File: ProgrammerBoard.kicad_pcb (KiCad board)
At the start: 2 copper layers, 11 parts, among them IC1 FT232RL, J1 USB_B_Micro, J2 Jumper_For_RJ45

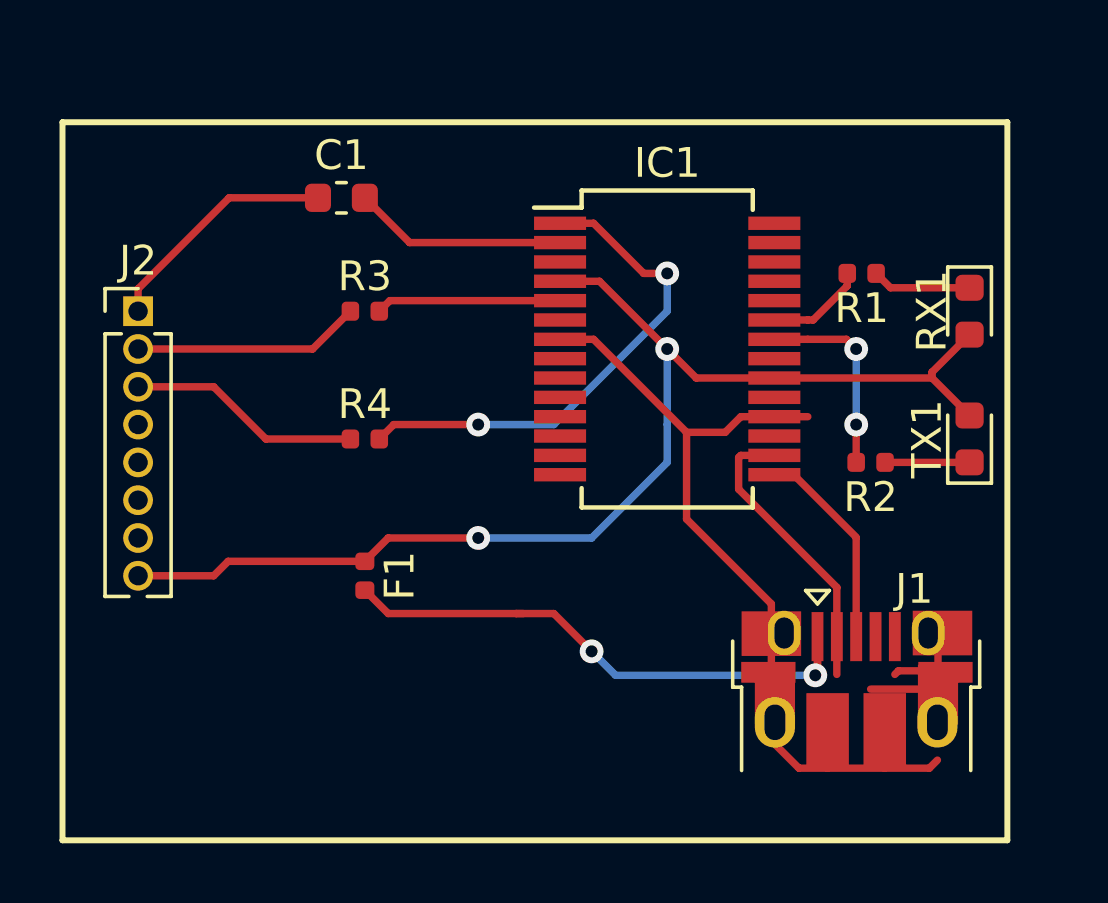
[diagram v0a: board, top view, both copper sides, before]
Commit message: Board size optimization
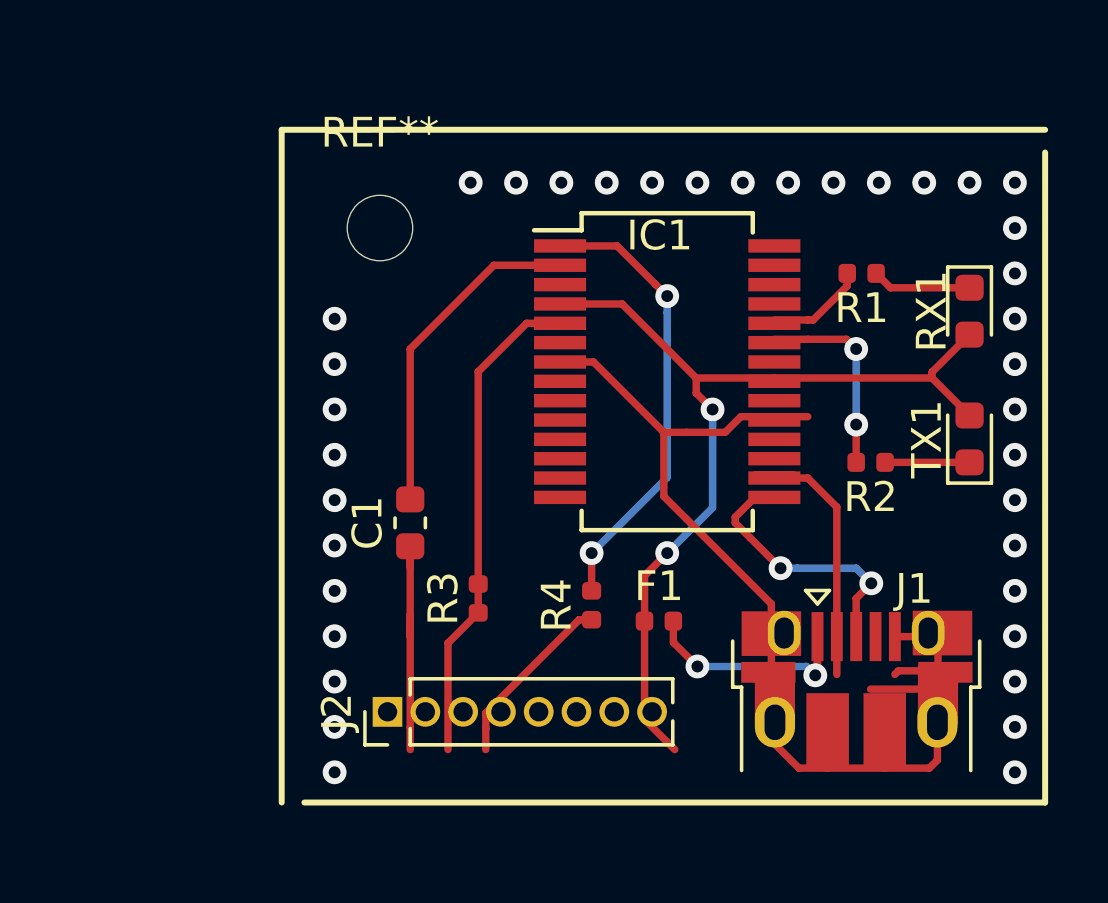
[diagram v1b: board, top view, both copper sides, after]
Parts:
- added REF**: MountingHole_2.2mm_M2, MountingHole:MountingHole_2.2mm_M2, F.Cu at (61.5, 40.4)
- moved J2 15.9 mm to (61.7, 56.6), turned to 90 degrees
- moved C1 11.2 mm to (62.5, 50.3), turned to 90 degrees
- moved R3 10.4 mm to (64.8, 52.8), turned to 90 degrees
- moved F1 10.00 mm to (70.8, 53.6), turned to 0 degrees
- moved R4 9.45 mm to (68.6, 53.1), turned to 90 degrees
- moved IC1 0.76 mm to (71.1, 45.2)
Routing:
- net Net-(F1-Pad2): track 19.0 -> 8.35 mm
- net +5V: track 40.8 -> 31.4 mm
- net Earth: track 34.0 -> 39.5 mm
- net Net-(IC1-Pad5): track 6.22 -> 11.3 mm
- net Net-(C1-Pad2): track 7.18 -> 11.3 mm
- net Net-(J2-Pad2): track 7.66 -> 4.66 mm
- net Net-(IC1-Pad15): track 7.58 -> 9.49 mm, vias 0 -> 2
- net Net-(J2-Pad3): track 7.86 -> 6.08 mm
- net Net-(IC1-Pad1): track 17.0 -> 15.3 mm
- net GNDREF: vias 0 -> 37

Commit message: Finished Rev 0.0.1
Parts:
- added ?: MountingHole_2.2mm_M2, MountingHole:MountingHole_2.2mm_M2, F.Cu at (80.5, 56.6)
- added ?: MountingHole_2.2mm_M2, MountingHole:MountingHole_2.2mm_M2, F.Cu at (59.9, 56.4)
- added ?: MountingHole_2.2mm_M2, MountingHole:MountingHole_2.2mm_M2, F.Cu at (80.3, 38.1)
- added G***: LOGO, Libraries:LOGO_black, B.Cu at (70.9, 46.2)
- moved R3 7.71 mm to (62.5, 45.5)
- moved J2 6.06 mm to (58.4, 51.6), turned to 180 degrees
- moved J1 4.82 mm to (72.7, 56.4)
- moved ? 2.75 mm to (59.9, 38.1)
- moved F1 1.61 mm to (71.4, 52.1), turned to 270 degrees
- moved C1 1.47 mm to (63.2, 51.6), turned to 0 degrees
- moved R4 1.11 mm to (67.6, 52.6), turned to 0 degrees
- renumbered REF** to ?
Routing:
- net Earth: track 39.5 -> 29.3 mm
- net Net-(F1-Pad2): track 8.35 -> 2.05 mm, vias 2 -> 0
- net Net-(IC1-Pad5): track 11.3 -> 5.63 mm
- net Net-(C1-Pad1): track 8.11 -> 4.01 mm
- net Net-(J2-Pad3): track 6.08 -> 10.2 mm, vias 0 -> 2
- net Net-(J2-Pad2): track 4.66 -> 7.49 mm, vias 0 -> 2
- net Net-(IC1-Pad15): track 9.49 -> 6.67 mm, vias 2 -> 0
- net +5V: track 31.4 -> 33.4 mm
- net Net-(C1-Pad2): track 11.3 -> 12.5 mm, vias 0 -> 2
- net GNDREF: vias 37 -> 71
- added copper zone on B.Cu, net GNDREF
- added copper zone on F.Cu, net GNDREF
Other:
- board outline added: 27.4 x 25.4 mm
- board text added: "Programmer Board Created by Jack Kufa For MST URT"
- board text added: "Rev 0.0.1 Rev Date 10-10-18"

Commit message: Finished Rev 0.0.2
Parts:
- removed ? (x4): MountingHole_2.2mm_M2, MountingHole:MountingHole_2.2mm_M2
- removed G***: LOGO, Libraries:LOGO_black
- added REF**: MountingHole_2.2mm_M2_DIN965, MountingHole:MountingHole_2.2mm_M2_DIN965, F.Cu at (80.0, 38.8)
- added REF**: MountingHole_2.2mm_M2_DIN965, MountingHole:MountingHole_2.2mm_M2_DIN965, F.Cu at (60.5, 38.6)
- added REF**: MountingHole_2.2mm_M2_DIN965, MountingHole:MountingHole_2.2mm_M2_DIN965, F.Cu at (60.2, 56.1)
- added REF**: MountingHole_2.2mm_M2_DIN965, MountingHole:MountingHole_2.2mm_M2_DIN965, F.Cu at (79.8, 56.4)
- F1: value 500mA -> 2A
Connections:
- IC1 pad 18: Earth -> GNDREF
- IC1 pad 21: Earth -> GNDREF
- IC1 pad 25: Earth -> GNDREF
- IC1 pad 26: Earth -> GNDREF
- IC1 pad 7: Earth -> GNDREF
- J1 pad 5: Earth -> GNDREF
- J1 pad 6: Earth -> GNDREF
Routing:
- net Earth: track 29.3 -> 0.00 mm
- net GNDREF: track 0.00 -> 26.6 mm, vias 71 -> 37
- net Net-(IC1-Pad22): track 6.69 -> 5.93 mm
- net Net-(IC1-Pad23): track 3.34 -> 4.00 mm
- net (no net): vias 0 -> 2

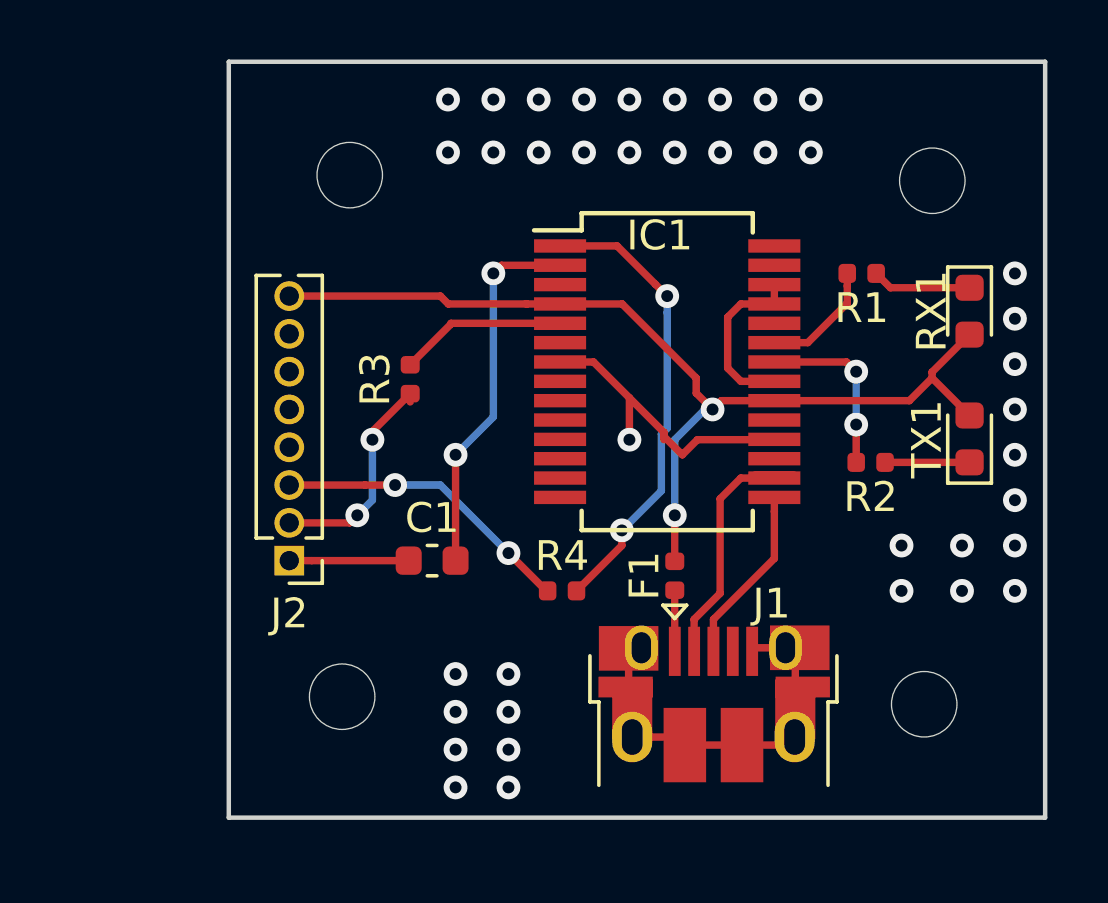
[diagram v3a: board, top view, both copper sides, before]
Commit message: Updated resistor sizes
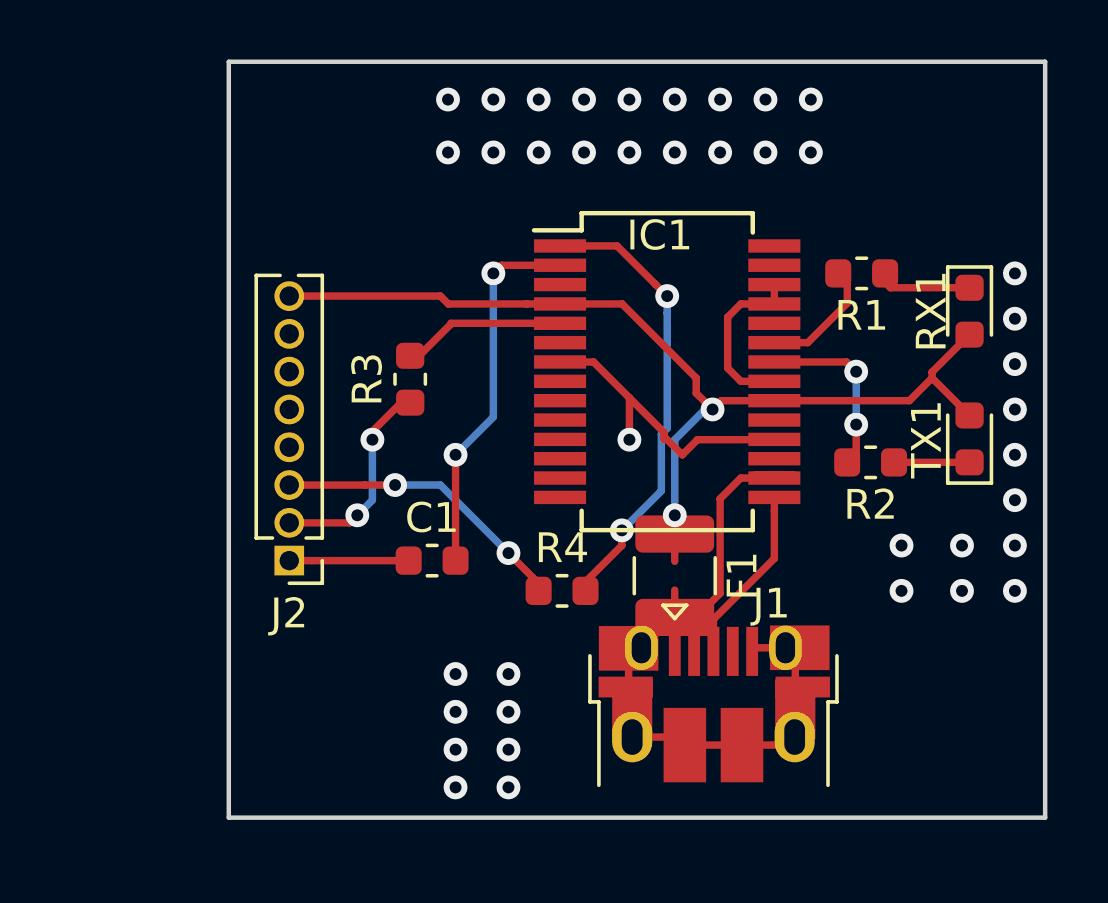
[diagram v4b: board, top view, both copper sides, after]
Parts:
- removed REF** (x4): MountingHole_2.2mm_M2_DIN965, MountingHole:MountingHole_2.2mm_M2_DIN965
- F1: footprint Fuse:Fuse_0402_1005Metric -> Fuse:Fuse_1210_3225Metric
- R1, R2, R3, R4: footprint Resistor_SMD:R_0402_1005Metric -> Resistor_SMD:R_0603_1608Metric

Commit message: S1.0.1 B1.0.1
Schematic:
* Add filter cap for 5v
* slight layout changes
* change gndref symbols to gnd

Board:
* slight via rework
* reworked ground planes
* increased 5v trace size
* moved fuse
* moved title to top
* add header label
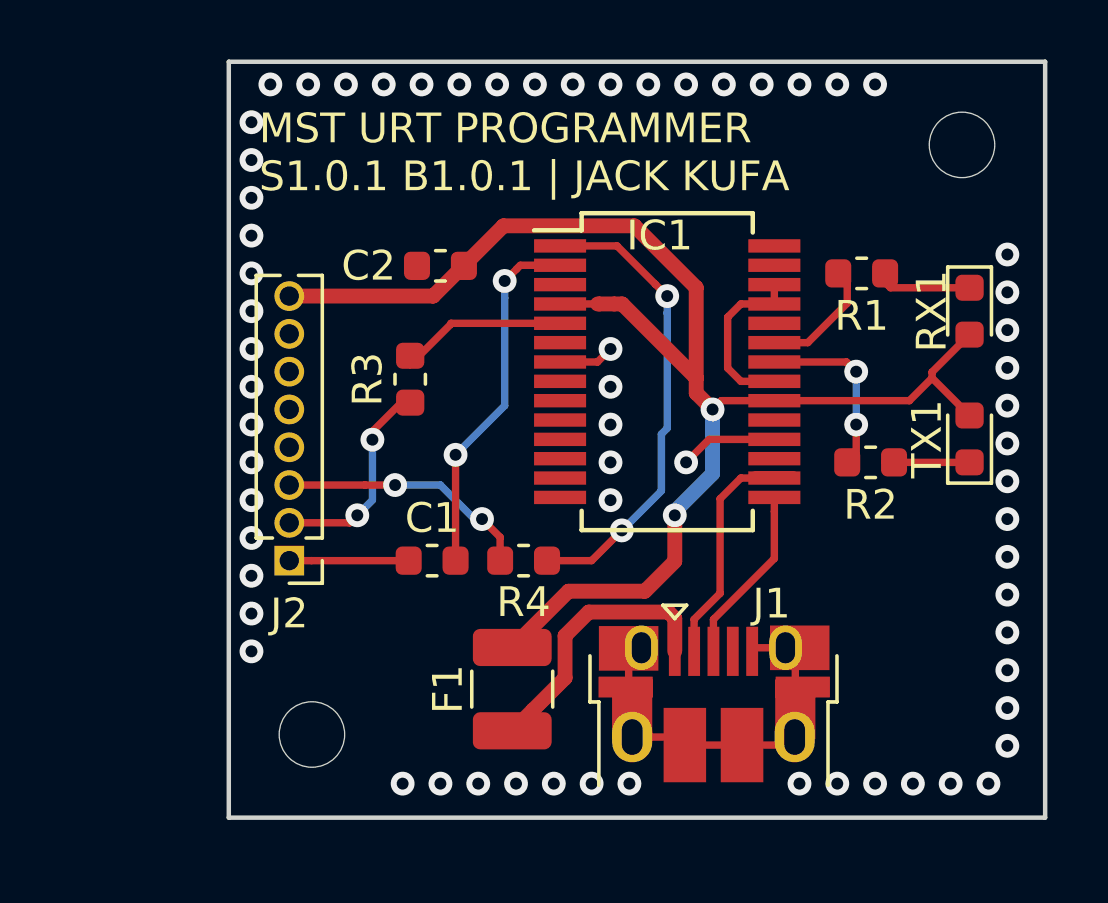
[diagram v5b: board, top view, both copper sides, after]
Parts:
- added C2: 100nF, Capacitor_SMD:C_0603_1608Metric, F.Cu at (63.5, 41.7)
- added REF**: MountingHole_2.2mm_M2, MountingHole:MountingHole_2.2mm_M2, F.Cu at (81.0, 37.6)
- added REF**: MountingHole_2.2mm_M2, MountingHole:MountingHole_2.2mm_M2, F.Cu at (59.2, 57.4)
- moved F1 6.66 mm to (65.9, 55.9)
- moved R4 1.64 mm to (66.3, 51.6)
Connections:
- net GNDREF renamed GND
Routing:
- net +5V: track 33.5 -> 49.9 mm
- net Net-(F1-Pad2): track 2.05 -> 9.14 mm
- net GND: track 26.6 -> 21.4 mm, vias 37 -> 65
- net Net-(J2-Pad3): track 10.2 -> 8.73 mm
- net (no net): vias 2 -> 0
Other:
- board text added: "MST URT PROGRAMMER S1.0.1 B1.0.1 | JACK KUFA"
